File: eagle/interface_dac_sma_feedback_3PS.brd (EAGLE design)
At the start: 95.5 x 139.1 mm, 31 parts, among them IC1 ISO1540, T1 TIP122V, T2 TIP122V, T3 TIP122V, X1 BU-SMA-V

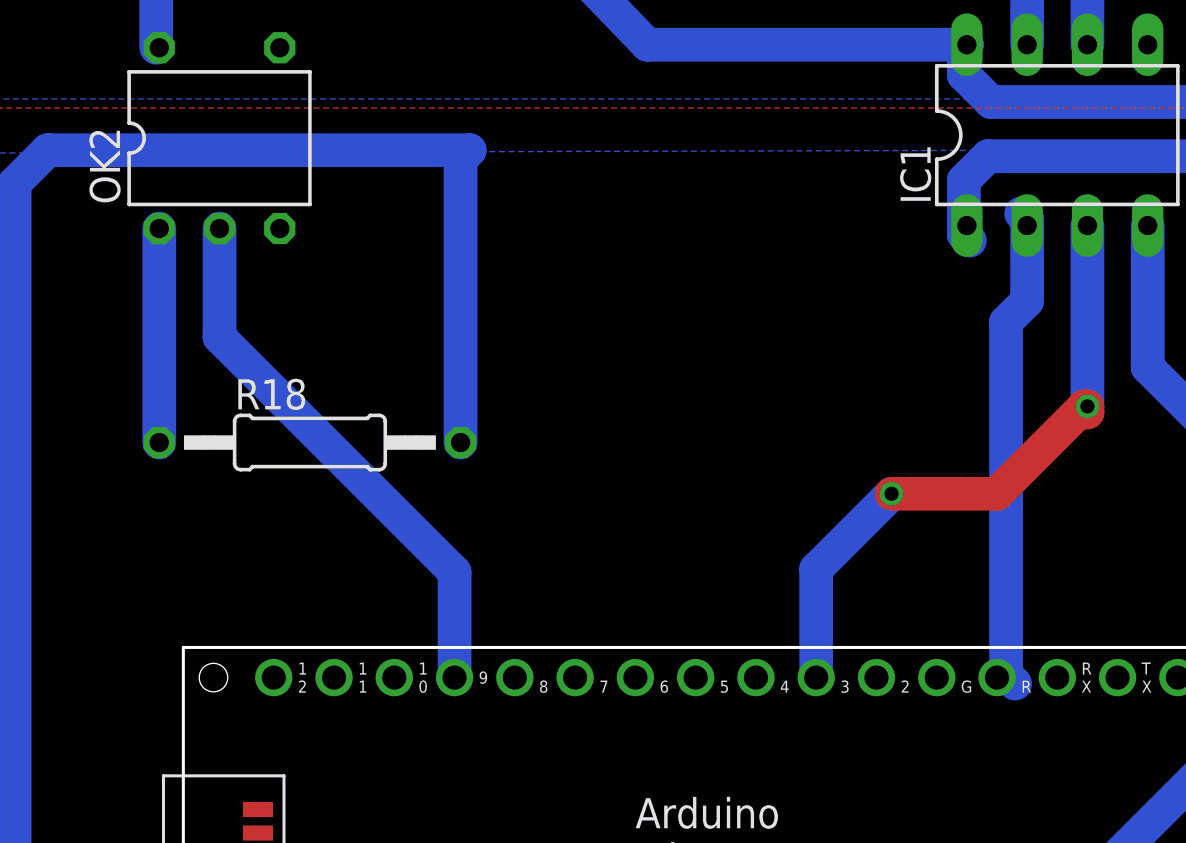
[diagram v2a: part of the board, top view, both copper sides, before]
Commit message: layout fixes
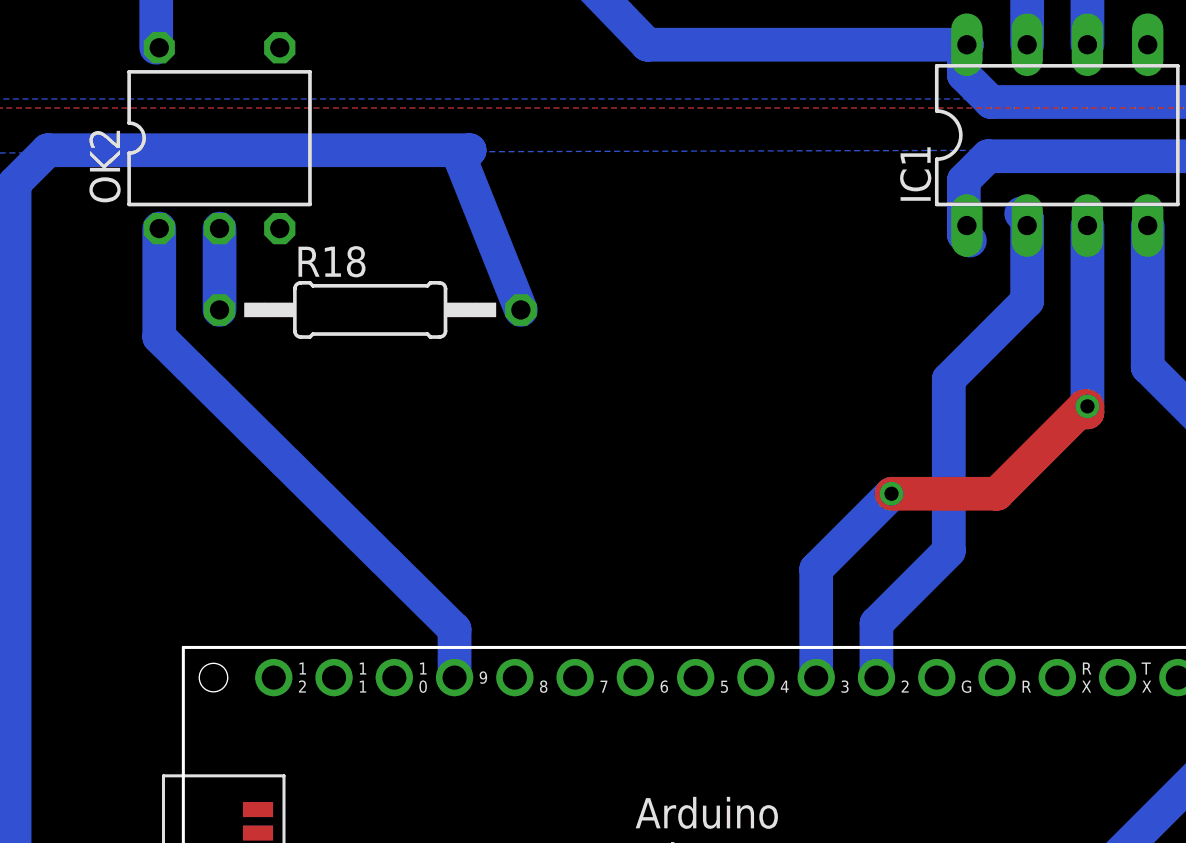
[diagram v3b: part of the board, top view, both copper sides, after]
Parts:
- moved R18 6.14 mm to (19.7, 38.0)
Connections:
- net N$7: now also OK2.2; no longer OK2.1
- net PWM9: now also OK2.1; no longer OK2.2
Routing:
- net N$7: track 9.02 -> 3.43 mm
- net AGND: track 159.2 -> 154.1 mm
- net SDA: track 20.4 -> 22.3 mm
- net PWM9: track 23.0 -> 24.1 mm
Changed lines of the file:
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@@
 <attribute name="OC_FARNELL" value="unknown" x="88.5952" y="75.4126" size="1.778" layer="27" rot="R180" display="off"/>
 </element>
-<element name="R18" library="rcl" package="0207/12" value="100" x="17.145" y="32.385"/>
+<element name="R18" library="rcl" package="0207/12" value="100" x="19.685" y="37.973"/>
 <element name="CONTROLGD2" library="con-molex" package="KK-156-2" value="" x="10.668" y="74.422" rot="R90">
 <attribute name="OC_NEWARK" value="unknown" x="10.668" y="74.422" size="1.778" layer="27" rot="R90" display="off"/>
@@
 <wire x1="48.641" y1="12.446" x2="48.641" y2="7.239" width="1.4224" layer="16"/>
 <wire x1="48.641" y1="7.239" x2="48.641" y2="6.985" width="1.4224" layer="16"/>
-<wire x1="23.495" y1="32.385" x2="23.495" y2="44.323" width="1.4224" layer="16"/>
+<wire x1="26.035" y1="37.973" x2="23.495" y2="44.323" width="1.4224" layer="16"/>
 <wire x1="23.495" y1="44.323" x2="23.876" y2="44.704" width="1.4224" layer="16"/>
 <wire x1="23.876" y1="44.704" x2="6.096" y2="44.704" width="1.4224" layer="16"/>
@@
 <contactref element="PCB1" pad="D2"/>
 <contactref element="IC1" pad="2"/>
-<wire x1="46.482" y1="37.465" x2="46.482" y2="22.606" width="1.4224" layer="16"/>
-<wire x1="46.482" y1="22.606" x2="46.863" y2="22.225" width="1.4224" layer="16"/>
-<wire x1="46.482" y1="37.465" x2="47.371" y2="38.354" width="1.4224" layer="16"/>
+<wire x1="41.021" y1="24.765" x2="41.021" y2="22.479" width="1.4224" layer="16"/>
+<wire x1="44.069" y1="35.052" x2="47.371" y2="38.354" width="1.4224" layer="16"/>
 <wire x1="47.371" y1="38.354" x2="47.371" y2="41.783" width="1.4224" layer="16"/>
 <wire x1="47.371" y1="41.783" x2="47.117" y2="42.037" width="1.4224" layer="16"/>
+<wire x1="41.021" y1="24.765" x2="44.069" y2="27.813" width="1.4224" layer="16"/>
+<wire x1="44.069" y1="27.813" x2="44.069" y2="35.052" width="1.4224" layer="16"/>
 <wire x1="47.371" y1="41.783" x2="47.371" y2="41.529" width="0" layer="19" extent="16-16"/>
-<wire x1="41.021" y1="22.479" x2="46.482" y2="22.606" width="0" layer="19" extent="16-16"/>
 </signal>
 <signal name="PWM9">
 <contactref element="PCB1" pad="D9"/>
-<contactref element="OK2" pad="2"/>
-<wire x1="13.335" y1="41.402" x2="13.335" y2="36.83" width="1.4224" layer="16"/>
-<wire x1="13.335" y1="36.83" x2="23.241" y2="26.924" width="1.4224" layer="16"/>
-<wire x1="23.241" y1="26.924" x2="23.241" y2="22.479" width="1.4224" layer="16"/>
+<wire x1="10.795" y1="36.83" x2="23.241" y2="24.511" width="1.4224" layer="16"/>
+<wire x1="23.241" y1="24.511" x2="23.241" y2="22.479" width="1.4224" layer="16"/>
+<contactref element="OK2" pad="1"/>
+<wire x1="10.795" y1="36.83" x2="10.795" y2="41.402" width="1.4224" layer="16"/>
 </signal>
 <signal name="N$12">
@@
 <wire x1="81.153" y1="75.438" x2="88.3158" y2="75.438" width="1.4224" layer="16"/>
 <wire x1="88.3158" y1="75.438" x2="88.5952" y2="75.4126" width="1.4224" layer="16"/>
-</signal>
-<signal name="N$7">
-<contactref element="R18" pad="1"/>
-<contactref element="OK2" pad="1"/>
-<wire x1="10.795" y1="41.402" x2="10.795" y2="32.385" width="1.4224" layer="16"/>
 </signal>
 <signal name="ENSW2">
@@
 <wire x1="59.944" y1="90.424" x2="60.071" y2="90.551" width="2.1844" layer="16"/>
 </signal>
+<signal name="N$7">
+<contactref element="OK2" pad="2"/>
+<contactref element="R18" pad="1"/>
+<wire x1="13.335" y1="37.973" x2="13.335" y2="41.402" width="1.4224" layer="16"/>
+</signal>
 </signals>

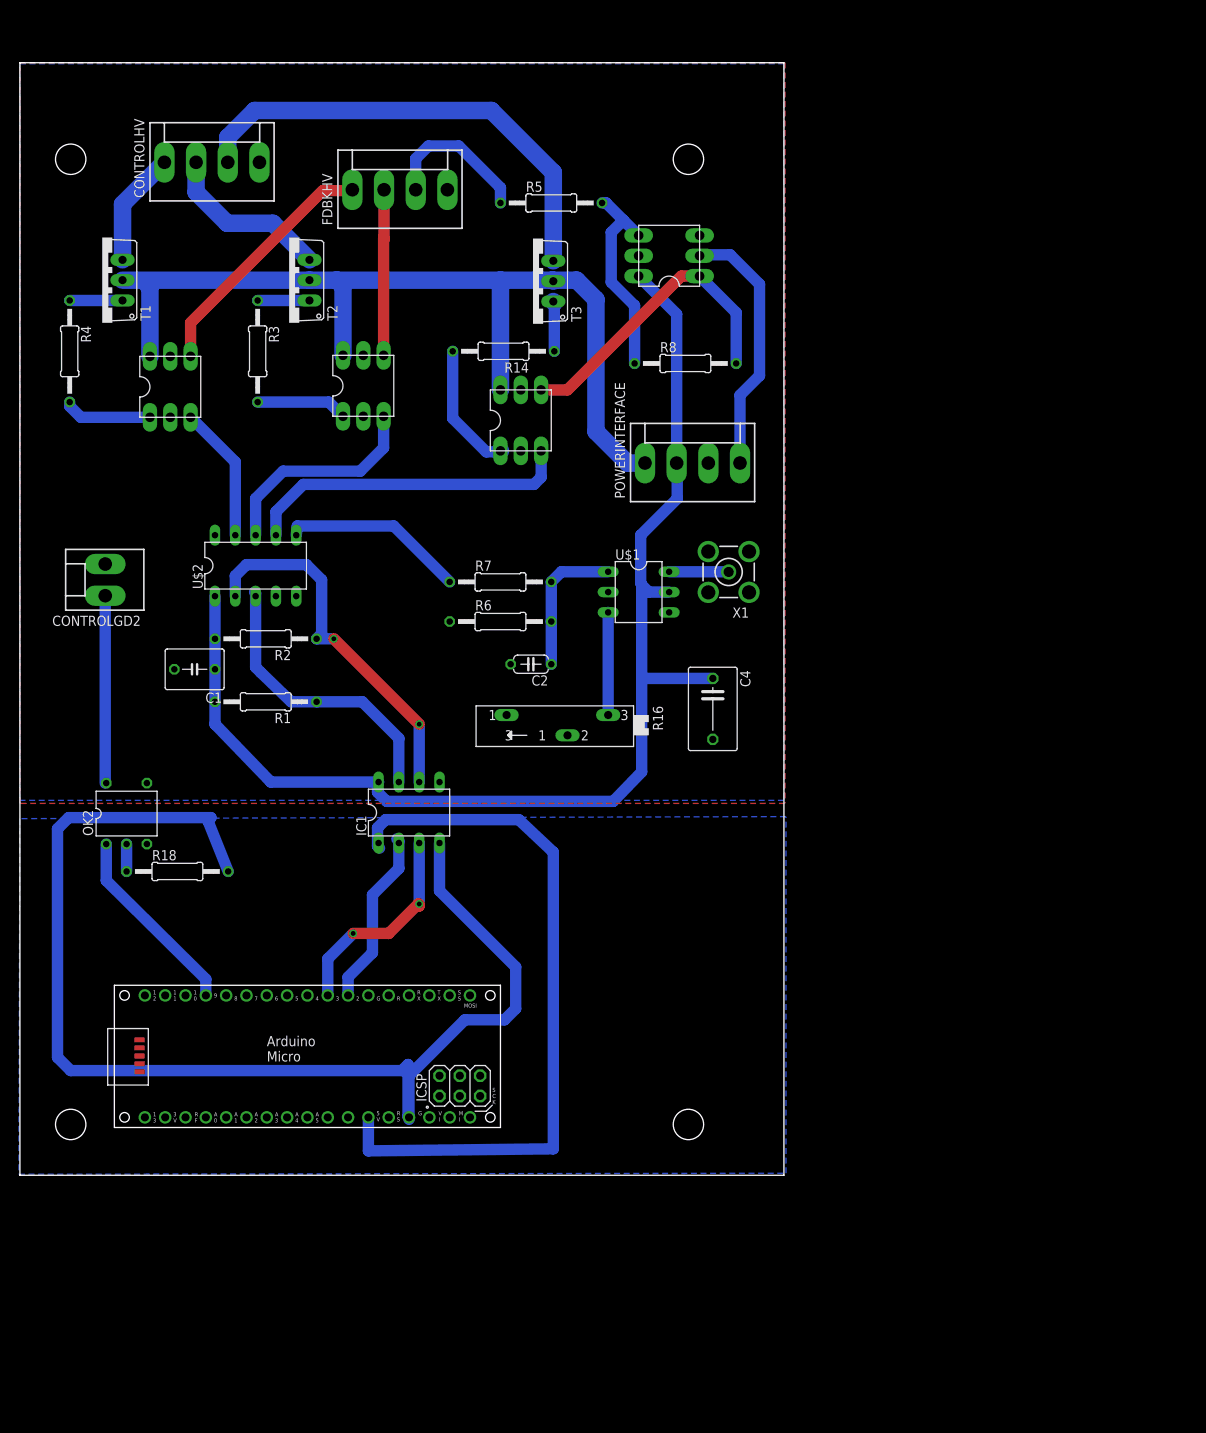
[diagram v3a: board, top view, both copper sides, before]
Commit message: use lt1352 opamp for feedback, smd output up to 1.6kVpp
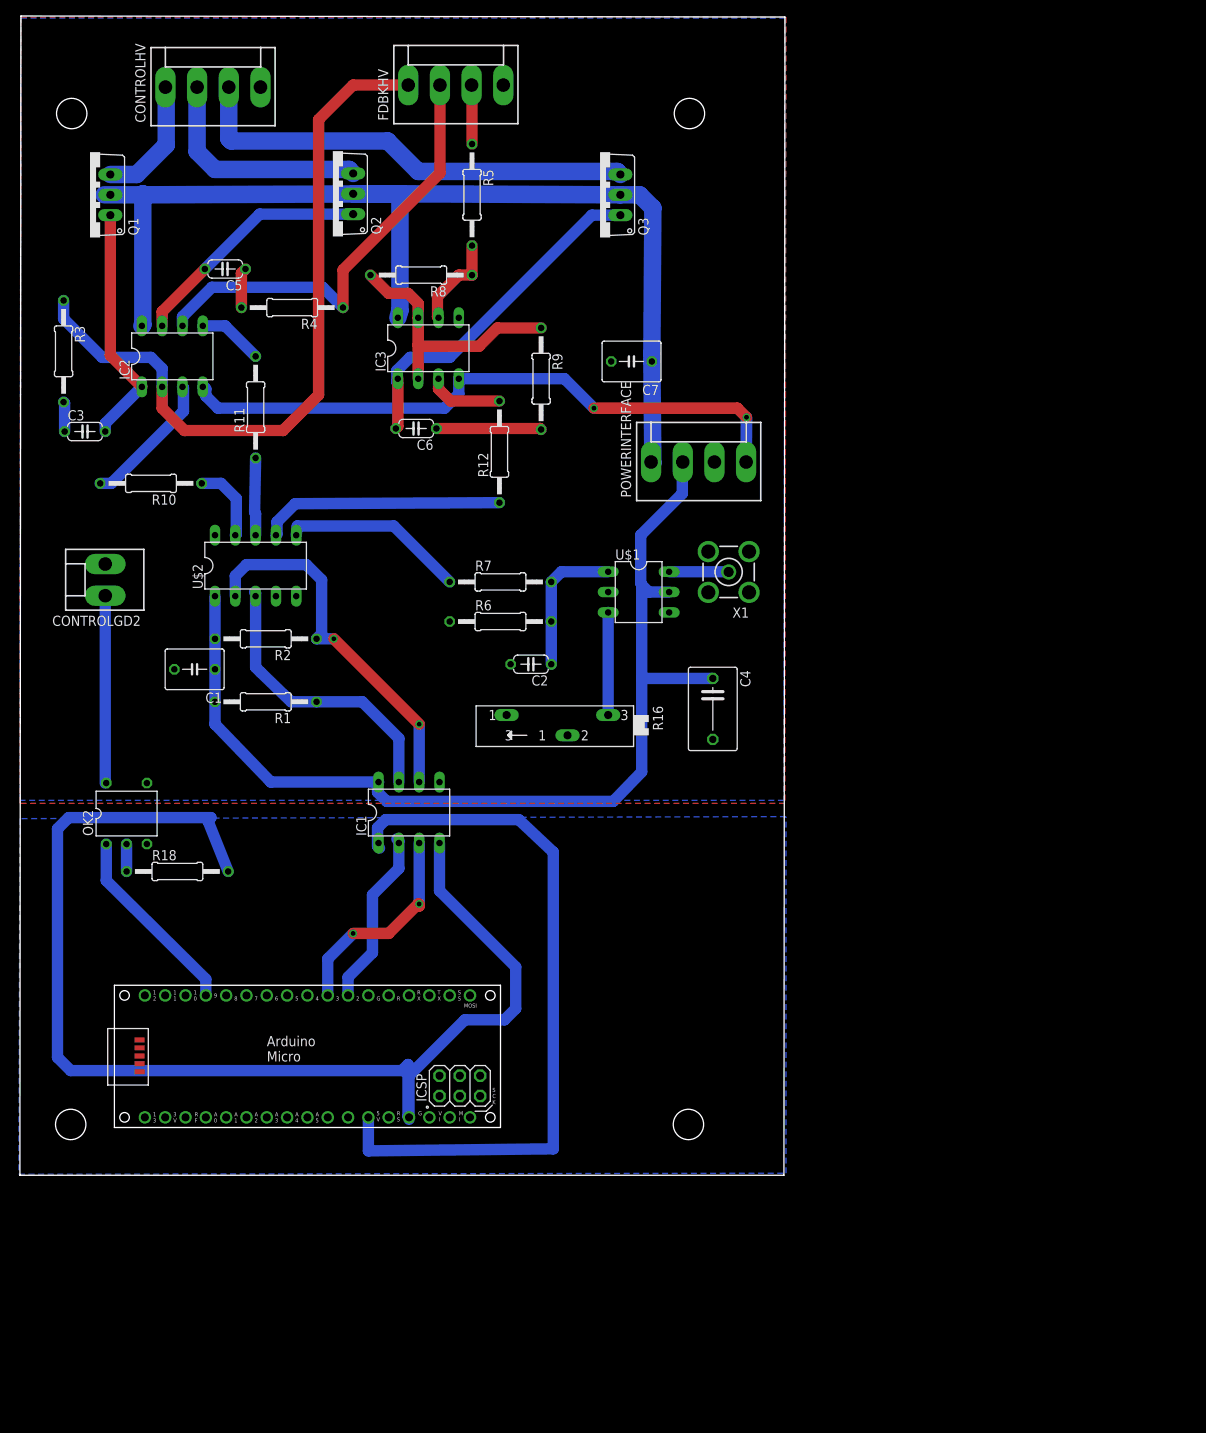
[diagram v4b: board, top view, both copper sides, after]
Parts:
- removed R14: 1k, resistor:0207/12
- removed T1, T2, T3: TIP122V, transistor-npn:TO220V
- removed U$3, U$4, U$5, U$6: OPA735DIL, texas:DIL6
- added C3, C5, C6: (no value), resistor:C050-024X044
- added C7: (no value), resistor:C050-050X075
- added IC2, IC3: LT1352PA, linear-technology:DIL08
- added Q1, Q2, Q3: TIP122V, transistor-npn:TO220V
- added R10, R11: 20k, resistor:0207/12
- added R12: 12, resistor:0207/12
- added R9: (no value), resistor:0207/12
- FDBKHV: value (none) -> 40k
- R3, R4: value 1k -> (none)
- R5, R8: value 1k -> 20k
- moved R8 34.8 mm to (50.2, 112.5), turned to 180 degrees
- moved R4 28.3 mm to (34.0, 108.5), turned to 180 degrees
- moved R3 24.3 mm to (5.46, 103.0)
- moved FDBKHV 14.8 mm to (54.5, 136.3)
- moved R5 9.96 mm to (56.5, 122.6), turned to 270 degrees
- moved CONTROLHV 9.40 mm to (24.1, 136.0)
- moved POWERINTERFACE 0.77 mm to (84.8, 89.2)
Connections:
- new net N$24: R10.1, U$2.9
- new net N$25: R12.1, U$2.7
- new net N$26: R11.1, U$2.8
- net +12V: now also C7.1, IC2.8, IC3.8, Q1.2, Q2.2, Q3.2; no longer T1.2, T2.2, T3.2, U$4.P$6, U$5.P$6, U$6.P$6
- net -5V: now also IC2.4, IC3.4; no longer U$3.P$2
- net GND: now also C7.2, IC3.5; no longer U$3.P$3, U$4.P$2, U$5.P$2, U$6.P$2
- net N$10: now also C5.2, IC2.7, Q2.1; no longer R3.2, U$5.P$1
- net N$11: now also Q2.3; no longer T2.3
- net N$14: now also IC3.2, IC3.7, R9.1; no longer U$3.P$1, U$4.P$4
- net N$15: now also C5.1, R4.2; no longer R14.1, T3.1
- net N$16: now also IC2.3, R10.2; no longer U$2.9, U$6.P$3
- net N$17: now also IC2.5, R11.2; no longer U$2.8, U$5.P$3
- net N$18: now also IC3.3, R12.2; no longer U$2.7, U$4.P$3
- net N$19: now also C3.2, IC2.1, Q1.1; no longer R4.2, U$6.P$1
- net N$20: now also C6.1, R9.2; no longer R3.1, T2.1
- net N$21: now also C6.2, IC3.1, Q3.1; no longer R14.2, U$4.P$1
- net N$23: now also IC3.6; no longer U$3.P$4
- net N$3: now also C3.1, R3.2; no longer R4.1, T1.1
- net N$4: now also Q1.3; no longer T1.3
- net N$5: now also Q3.3; no longer T3.3
- net N$6: now also IC2.6, R4.1; no longer U$5.P$4
- net N$8: now also IC2.2, R3.1; no longer U$6.P$4
- net VCC: no longer U$3.P$6
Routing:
- net N$8: track 31.3 -> 92.1 mm
- net -5V: track 32.4 -> 85.4 mm, vias 0 -> 2
- net N$6: track 21.1 -> 56.6 mm
- net N$18: track 41.2 -> 9.52 mm
- net N$25: track 0.00 -> 30.5 mm
- net N$21: track 16.1 -> 43.9 mm
- net VCC: track 154.5 -> 130.4 mm
- net +12V: track 117.2 -> 139.9 mm
- net N$19: track 11.1 -> 30.6 mm
- net N$10: track 11.4 -> 30.7 mm
- net N$17: track 27.1 -> 8.18 mm
- net N$23: track 26.0 -> 11.8 mm
- net N$9: track 19.2 -> 7.39 mm
- net N$24: track 0.00 -> 9.73 mm
- net N$26: track 0.00 -> 9.68 mm
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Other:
- board size 95.5 x 139.1 mm -> 95.6 x 144.9 mm

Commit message: update component values
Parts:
- C3, C4, C5, C6, C7: value (none) -> 10n
- FDBKHV: value 40k -> (none)
- R3, R4, R9: value (none) -> 10k
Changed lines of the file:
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@@
 <element name="PCB1" library="E14_Arduino_published" package="ARDUINO_MICRO" value="ARDUINO_MICRO" x="11.811" y="5.969"/>
 <element name="U$1" library="linear-technology" package="DIL06" value="LTC6992" x="77.343" y="72.898" rot="R270"/>
-<element name="C4" library="resistor" package="C075-063X106" value="" x="86.614" y="58.293" rot="R270"/>
+<element name="C4" library="resistor" package="C075-063X106" value="10n" x="86.614" y="58.293" rot="R270"/>
 <element name="R16" library="pot" package="SP19L" value="" x="66.548" y="56.261" rot="R180"/>
 <element name="X1" library="con-coax" package="BU-SMA-V" value="BU-SMA-V" x="88.5952" y="75.4126" rot="R180">
@@
 <attribute name="OC_FARNELL" value="unknown" x="24.13" y="136.017" size="1.778" layer="27" display="off"/>
 </element>
-<element name="FDBKHV" library="con-molex" package="KK-156-4" value="40k" x="54.483" y="136.271">
+<element name="FDBKHV" library="con-molex" package="KK-156-4" value="" x="54.483" y="136.271">
 <attribute name="OC_NEWARK" value="unknown" x="54.483" y="136.271" size="1.778" layer="27" display="off"/>
 <attribute name="MPN" value="" x="54.483" y="136.271" size="1.778" layer="27" display="off"/>
@@
 <element name="R5" library="resistor" package="0207/12" value="20k" x="56.515" y="122.555" rot="R270"/>
 <element name="R8" library="resistor" package="0207/12" value="20k" x="50.165" y="112.522" rot="R180"/>
-<element name="R3" library="resistor" package="0207/12" value="" x="5.461" y="102.997" rot="R270"/>
-<element name="C3" library="resistor" package="C050-024X044" value="" x="8.128" y="92.964"/>
-<element name="R4" library="resistor" package="0207/12" value="" x="34.036" y="108.458" rot="R180"/>
-<element name="C5" library="resistor" package="C050-024X044" value="" x="25.654" y="113.284" rot="R180"/>
-<element name="R9" library="resistor" package="0207/12" value="" x="65.151" y="99.568" rot="R270"/>
-<element name="C6" library="resistor" package="C050-024X044" value="" x="49.53" y="93.345" rot="R180"/>
-<element name="C7" library="resistor" package="C050-050X075" value="" x="76.454" y="101.727" rot="R180"/>
+<element name="R3" library="resistor" package="0207/12" value="10k" x="5.461" y="102.997" rot="R270"/>
+<element name="C3" library="resistor" package="C050-024X044" value="10n" x="8.128" y="92.964"/>
+<element name="R4" library="resistor" package="0207/12" value="10k" x="34.036" y="108.458" rot="R180"/>
+<element name="C5" library="resistor" package="C050-024X044" value="10n" x="25.654" y="113.284" rot="R180"/>
+<element name="R9" library="resistor" package="0207/12" value="10k" x="65.151" y="99.568" rot="R270"/>
+<element name="C6" library="resistor" package="C050-024X044" value="10n" x="49.53" y="93.345" rot="R180"/>
+<element name="C7" library="resistor" package="C050-050X075" value="10n" x="76.454" y="101.727" rot="R180"/>
 <element name="R10" library="resistor" package="0207/12" value="20k" x="16.383" y="86.487" rot="R180"/>
 <element name="R11" library="resistor" package="0207/12" value="20k" x="29.464" y="96.012" rot="R90"/>

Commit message: Update values, code
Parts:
- R10, R11: value 20k -> 10k
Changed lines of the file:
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@@
 <element name="C6" library="resistor" package="C050-024X044" value="10n" x="49.53" y="93.345" rot="R180"/>
 <element name="C7" library="resistor" package="C050-050X075" value="10n" x="76.454" y="101.727" rot="R180"/>
-<element name="R10" library="resistor" package="0207/12" value="20k" x="16.383" y="86.487" rot="R180"/>
-<element name="R11" library="resistor" package="0207/12" value="20k" x="29.464" y="96.012" rot="R90"/>
+<element name="R10" library="resistor" package="0207/12" value="10k" x="16.383" y="86.487" rot="R180"/>
+<element name="R11" library="resistor" package="0207/12" value="10k" x="29.464" y="96.012" rot="R90"/>
 <element name="R12" library="resistor" package="0207/12" value="12" x="59.944" y="90.424" rot="R90"/>
 <element name="Q1" library="transistor-npn" package="TO220V" value="TIP122V" x="8.763" y="122.555" rot="R90"/>
